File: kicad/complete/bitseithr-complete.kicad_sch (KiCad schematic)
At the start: 26 parts, among them IC1 AY-3-8912_28PIN, IC2 AY-3-8912_28PIN, J1 Power, J10 OLED Connector, J2 PWM, J3 Analog, J4 PWM, J5 Analog, J6 Communication, J7 Digital, J8 AUDIO JACK 1, J9 AUDIO JACK 2, SW1 POWER SWITCH

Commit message: schematic progress
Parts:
- removed R74: CLR, Resistor_THT:R_Axial_DIN0207_L6.3mm_D2.5mm_P10.16mm_Horizontal, symbol Device:R_Small_US
- added P1: TO KEYBOARD 1, EasyEDA_Lib:IDC-TH_20P-L33.0-W13.8-H-M-R2-C10-P2.54-S2.54-TR, symbol EasyEDA_Lib:IDC Box 2X10 2.54MM
- added R10: R_Small_US, symbol Device:R_Small_US
- added R9: 1kΩ, EasyEDA_Lib:RES-ADJ-TH_3296W, symbol EasyEDA_Lib:3296W-1-102LF
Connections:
- net 22 is gone; now on net DA0: J7.33 (Pin_33)
- net 23 is gone; now on net DA1: J7.34 (Pin_34)
- net 24 is gone; now on net DA2: J7.31 (Pin_31)
- net 25 is gone; now on net DA3: J7.32 (Pin_32)
- net 26 is gone; now on net DA4: J7.29 (Pin_29)
- net 27 is gone; now on net DA5: J7.30 (Pin_30)
- net 28 is gone; now on net DA6: J7.27 (Pin_27)
- net 29 is gone; now on net DA7: J7.28 (Pin_28)
- net A0 is gone; now on net BDIR-1: J3.1 (Pin_1)
- net A1 is gone; now on net BC1-1: J3.2 (Pin_2)
- net A2 is gone; now on net BDIR-2: J3.3 (Pin_3)
- net A3 is gone; now on net BC1-2: J3.4 (Pin_4)
- net Earth is gone; now on net GND: D73.1 (K), J8.S, J9.S, R4.2, R8.2
- net +5V: now also IC1.17 (A8), IC1.19 (BC2), IC2.19 (BC2), J10.2 (Pin_2)
- net +9V: now also P1.1
- net GND: now also IC1.6 (VSS), IC2.6 (VSS), J10.1 (Pin_1), P1.2
- net SCL/21: now also J10.4 (Pin_4)
- net SDA/20: now also J10.3 (Pin_3)
- net BDIR-1: now reaches IC1.18 (BDIR)
- net BC1-1: now reaches IC1.20 (BC1)
- net DA7: now reaches IC1.21 (DA7)
- net DA7: now also IC2.21 (DA7)
- net DA6: now reaches IC1.22 (DA6)
- net DA6: now also IC2.22 (DA6)
- net DA5: now reaches IC1.23 (DA5)
- net DA5: now also IC2.23 (DA5)
- net DA4: now reaches IC1.24 (DA4)
- net DA4: now also IC2.24 (DA4)
- net DA3: now reaches IC1.25 (DA3)
- net DA3: now also IC2.25 (DA3)
- net DA2: now reaches IC1.26 (DA2)
- net DA2: now also IC2.26 (DA2)
- net DA1: now reaches IC1.27 (DA1)
- net DA1: now also IC2.27 (DA1)
- net DA0: now reaches IC1.28 (DA0)
- net DA0: now also IC2.28 (DA0)
- net at D73.2 (A): now also R9.3
- net BDIR-2: now reaches IC2.18 (BDIR)
- net BC1-2: now reaches IC2.20 (BC1)
- new net: R10.1, R9.1, R9.2
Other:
- moved on the sheet: D73

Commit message: almost done with complete schematic
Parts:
- removed D73: POWER LED, LED_THT:LED_D3.0mm, symbol Device:LED_Small
- removed R9: 1kΩ, EasyEDA_Lib:RES-ADJ-TH_3296W, symbol EasyEDA_Lib:3296W-1-102LF
- added C25: 4.7uF-bi, Capacitor_THT:CP_Radial_D5.0mm_P2.00mm, symbol Device:CP1_Small
- added C3, C5, C8: 10 uF, Capacitor_THT:CP_Radial_D5.0mm_P2.50mm, symbol Device:CP1_Small
- added C4, C6, C7: .1 uF, caps-film:0.2_.MED, symbol Device:CP1_Small
- added J11: lil-joystick, cholm-footprints:Joystick-breakout-upside-down, symbol bit0wulf-0-rescue:psp-joystick-rect-clholm-kicad-lib
- added R13, R14, R9: 10k, symbol Device:R_Small_US
- added R22: 100k, Resistor_SMD:R_1206_3216Metric, symbol Device:R_Small_US
- added U1: ~, EasyEDA_Lib:SOIC-8_L4.9-W3.9-P1.27-LS6.0-BL, symbol EasyEDA_Lib:OPA1692IDR
- added U4: TL072, Package_SO:SOIC-8-1EP_3.9x4.9mm_P1.27mm_EP2.29x3mm, symbol Amplifier_Operational:TL072
- added VOLUME1: 100k-A, clholm-kicad-lib:16MM_T.MOUNT, symbol Device:R_POT_US
- P1: value TO KEYBOARD 1 -> SHIELD CONN 1
- R10: value R_Small_US -> 10k; now not fitted
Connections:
- net *10 is gone; now on net CLK: J2.8 (Pin_8)
- net *44 is gone; now on net ROW4: J7.11 (Pin_11)
- net *45 is gone; now on net ROW5: J7.12 (Pin_12)
- net 30 is gone; now on net RESET: J7.25 (Pin_25)
- net 31 is gone; now on net COL0: J7.26 (Pin_26)
- net 32 is gone; now on net COL1: J7.23 (Pin_23)
- net 33 is gone; now on net COL2: J7.24 (Pin_24)
- net 34 is gone; now on net COL3: J7.21 (Pin_21)
- net 35 is gone; now on net COL4: J7.22 (Pin_22)
- net 36 is gone; now on net COL5: J7.19 (Pin_19)
- net 37 is gone; now on net COL6: J7.20 (Pin_20)
- net 38 is gone; now on net COL7: J7.17 (Pin_17)
- net 39 is gone; now on net COL8: J7.18 (Pin_18)
- net 40 is gone; now on net ROW0: J7.15 (Pin_15)
- net 41 is gone; now on net ROW1: J7.16 (Pin_16)
- net 42 is gone; now on net ROW2: J7.13 (Pin_13)
- net 43 is gone; now on net ROW3: J7.14 (Pin_14)
- net VCC is gone; now on net +9V: J1.8 (Pin_8)
- net +5V: now also IC1.3 (VCC), IC2.3 (VCC), C3.1, C4.1, C6.1, C8.1, J11.1 (VCC)
- net +9V: now also C5.1, C7.1
- net BC1-1: now also R9.1
- net BC1-2: now also R13.1
- net BDIR-1: now also R10.1
- net BDIR-2: now also R14.1
- net GND: now also R10.2, C3.2, C4.2, C5.2, C6.2, C7.2, C8.2, J11.4 (GND), R13.2, R14.2, R9.2
- net CLK: now reaches IC1.15 (CLK)
- net CLK: now also IC2.15 (CLK)
- net RESET: now reaches IC1.16 (/RESET)
- net RESET: now also IC2.16 (/RESET)
- net COL1: now reaches P1.10
- net COL2: now reaches P1.11
- net COL3: now reaches P1.12
- net COL4: now reaches P1.13
- net COL5: now reaches P1.14
- net COL6: now reaches P1.15
- net COL7: now reaches P1.16
- net COL8: now reaches P1.17
- net ROW0: now reaches P1.3
- net ROW1: now reaches P1.4
- net ROW2: now reaches P1.5
- net ROW3: now reaches P1.6
- net ROW4: now reaches P1.7
- net ROW5: now reaches P1.8
- net COL0: now reaches P1.9
- net *2 renamed ECLK1
- net *3 renamed EDT1
- net +9V-IN renamed +9V IN
- net 48 renamed ESW1
- net 49 renamed ESW2
- net A4 renamed JOYX
- net JOYX: now also J11.3 (XOUT)
- net A5 renamed JOYY
- net JOYY: now also J11.2 (YOUT)
- net RX1/19 renamed EDT2
- net TX1/18 renamed ECLK2
- new net: R22.1, U4.6 (-), VOLUME1.3
- new net: C25.1, U4.7, VOLUME1.1, VOLUME1.2
- new net OUTPUT: C25.2
- new net VREF: U4.5 (+)
- no-connect marks 1 -> 5
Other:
- added sheet keyboard (keyboard.kicad_sch)
- company: (none) -> Offworld Serpent Devices
- title: (none) -> bitseithr synth
- moved on the sheet: C1, C2, D72, IC1, IC2, J8, J9, R1, R2, R3, R4, R5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

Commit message: more schematic updates
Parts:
- removed C1, C2: 100 uF, cholm-footprints:0801, symbol Device:CP1_Small
- removed C25: 4.7uF-bi, Capacitor_THT:CP_Radial_D5.0mm_P2.00mm, symbol Device:CP1_Small
- removed R22: 100k, Resistor_SMD:R_1206_3216Metric, symbol Device:R_Small_US
- removed U4: TL072, Package_SO:SOIC-8-1EP_3.9x4.9mm_P1.27mm_EP2.29x3mm, symbol Amplifier_Operational:TL072
- added C10, C12: 100uF, Capacitor_THT:CP_Radial_D6.3mm_P2.50mm, symbol Device:CP1_Small
- added C11, C13: 10uF, cholm-footprints:0801, symbol Device:CP1_Small
- added C18: .1uF, Capacitors:0805, symbol Device:C_Small
- added C21, C9: 10uF, Capacitor_THT:CP_Radial_D6.3mm_P2.50mm, symbol Device:CP1_Small
- added R15, R16: 100k, Resistor_SMD:R_1206_3216Metric, symbol Device:R_Small_US
- added R17, R18: 50k, Resistor_SMD:R_1206_3216Metric, symbol Device:R_Small_US
- added VOLUME2: 100k-A, clholm-kicad-lib:16MM_T.MOUNT, symbol Device:R_POT_US
- C3, C5, C8: value 10 uF -> 10uF
- C4, C6, C7: value .1 uF -> .1uF
- U1: value ~ -> OPA1692
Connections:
- net +5V: now also C18.1, R15.1
- net +9V: now also C9.1
- net GND: now also U1.4 (V-), C18.2, C21.2, C9.2, R16.2
- net at R1.1, R2.1, R3.1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: now also C11.1
- net OUTPUT-1: now reaches J8.T
- net OUTPUT-1: now also C10.2
- net at VOLUME1.3: now also U1.7 (OUT2), C12.1
- net at VOLUME1.1, VOLUME1.2: now also U1.6 (IN2-)
- net at U1.5 (IN2+): now also R18.1
- net at U1.1 (OUT1): now also C10.1, VOLUME2.3
- net at U1.2 (IN1-): now also VOLUME2.1, VOLUME2.2
- net at U1.3 (IN1+): now also R17.1
- net +2.5V: now reaches U1.8 (V+)
- net +2.5V: now also C21.1, R15.2, R16.1
- net at R5.1, R6.1, R7.1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: now also C13.1
- net OUTPUT-2: now reaches J9.T
- net OUTPUT-2: now also C12.2
- new net: C11.2, R17.2
- new net: C13.2, R18.2
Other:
- moved on the sheet: J11, J8, J9, U1A, U1B

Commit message: still workin. i'm crazy
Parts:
- removed C18: .1uF, Capacitors:0805, symbol Device:C_Small
- removed C9: 10uF, Capacitor_THT:CP_Radial_D6.3mm_P2.50mm, symbol Device:CP1_Small
- C21: value 10uF -> .1uF
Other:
- added sheet encoders (encoders.kicad_sch)
- moved on the sheet: C21, D72, R15, R16, SW1

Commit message: schematic continued
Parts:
- removed C21: .1uF, Capacitor_THT:CP_Radial_D6.3mm_P2.50mm, symbol Device:CP1_Small
- removed C4, C6, C7: .1uF, caps-film:0.2_.MED, symbol Device:CP1_Small
- removed R4, R8: 150R, symbol Device:R_Small_US
- added C1, C2, C4, C6: .1uF, symbol Device:C_Small
- R17, R18: value 50k -> 47k
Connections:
- net +2.5V: now also C1.1
- net +5V: now also C4.1, C6.1
- net +9V: now also C2.1
- net GND: now also C11.1, C13.1, R1.1, R2.1, R3.1, R5.1, R6.1, R7.1, C1.2, C2.2, C4.2, C6.2

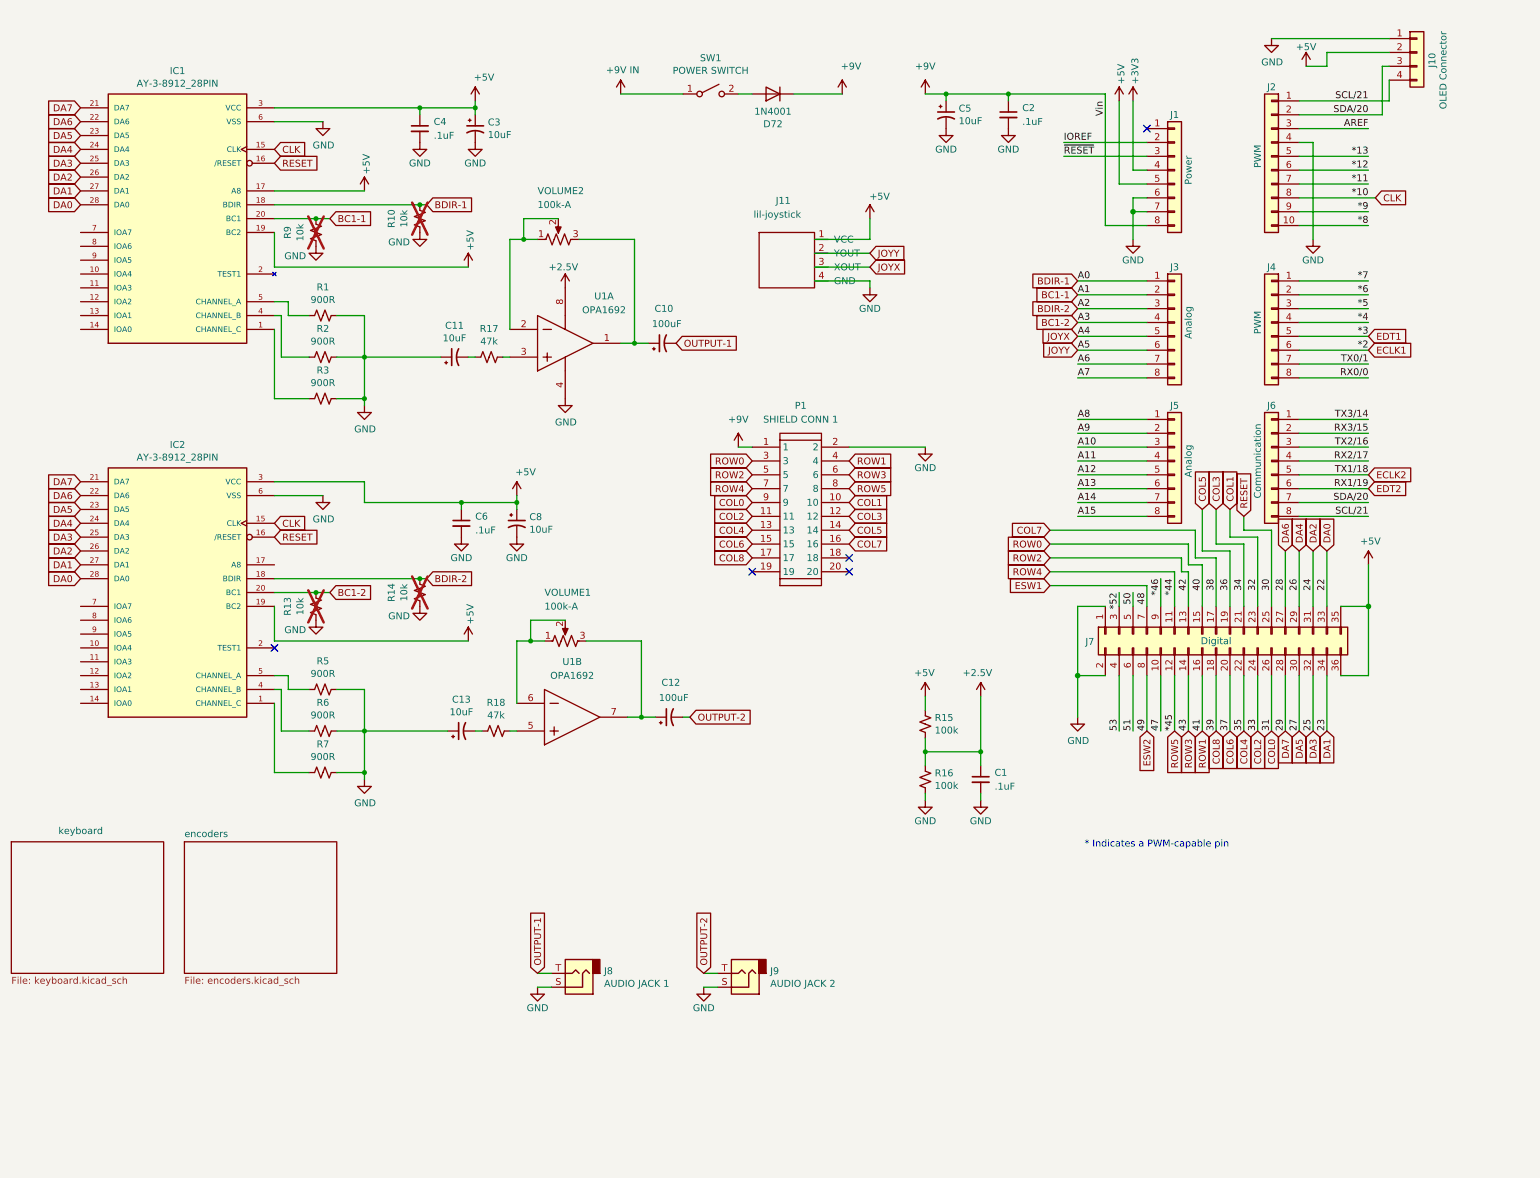
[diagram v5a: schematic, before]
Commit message: saving op-amp config before I mess with the feedback resistor
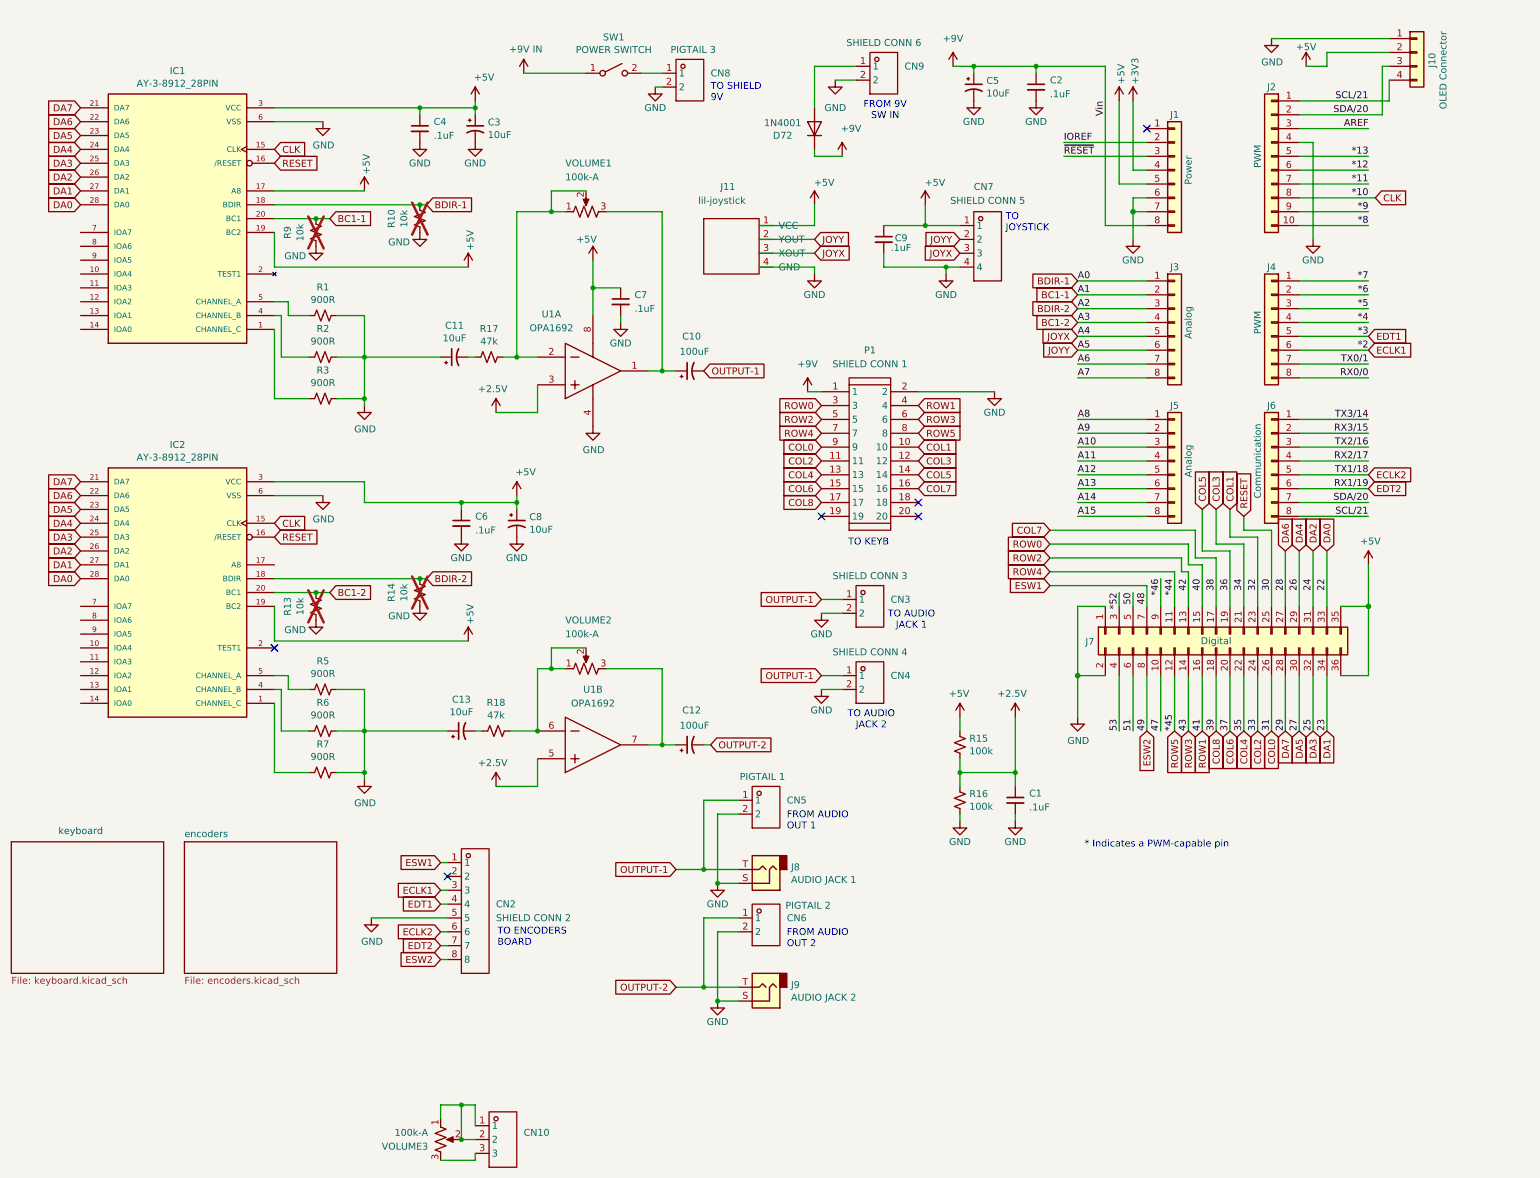
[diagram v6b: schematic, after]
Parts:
- added C7, C9: .1uF, symbol Device:C_Small
- added CN10: ~, EasyEDA_Lib:CONN-TH_3P-P2.50_HCTL_HC-XA-3AW, symbol EasyEDA_Lib:HC-XA-3AW
- added CN2: SHIELD CONN 2, EasyEDA_Lib:CONN-TH_8P-P2.50_HCTL_HC-XA-8AW, symbol EasyEDA_Lib:HC-XA-8AW
- added CN3: SHIELD CONN 3, EasyEDA_Lib:CONN-TH_2P-P2.50_HCTL_HC-XA-2AW, symbol EasyEDA_Lib:HC-XA-2AW
- added CN4: SHIELD CONN 4, EasyEDA_Lib:CONN-TH_2P-P2.50_HCTL_HC-XA-2AW, symbol EasyEDA_Lib:HC-XA-2AW
- added CN5: PIGTAIL 1, EasyEDA_Lib:CONN-TH_2P-P2.50_HCTL_HC-XA-2AW, symbol EasyEDA_Lib:HC-XA-2AW
- added CN6: PIGTAIL 2, EasyEDA_Lib:CONN-TH_2P-P2.50_HCTL_HC-XA-2AW, symbol EasyEDA_Lib:HC-XA-2AW
- added CN7: SHIELD CONN 5, EasyEDA_Lib:CONN-TH_4P-P2.50_HCTL_HC-XA-4AW, symbol EasyEDA_Lib:HC-XA-4AW
- added CN8: PIGTAIL 3, EasyEDA_Lib:CONN-TH_2P-P2.50_HCTL_HC-XA-2AW, symbol EasyEDA_Lib:HC-XA-2AW
- added CN9: SHIELD CONN 6, EasyEDA_Lib:CONN-TH_2P-P2.50_HCTL_HC-XA-2AW, symbol EasyEDA_Lib:HC-XA-2AW
- added VOLUME3: 100k-A, clholm-kicad-lib:16MM_T.MOUNT, symbol Device:R_POT_US
- renumbered VOLUME2 to VOLUME1, VOLUME1 to VOLUME2
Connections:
- net +2.5V: now also U1.3 (IN1+), U1.5 (IN2+); no longer U1.8 (V+)
- net +5V: now also U1.8 (V+), C7.1, C9.1, CN7.1
- net ECLK1: now also CN2.3
- net ECLK2: now also CN2.6
- net EDT1: now also CN2.4
- net EDT2: now also CN2.7
- net ESW1: now also CN2.1
- net ESW2: now also CN2.8
- net GND: now also C7.2, C9.2, CN2.5, CN3.2, CN4.2, CN5.2, CN6.2, CN7.4, CN8.2, CN9.2
- net JOYX: now also CN7.3
- net JOYY: now also CN7.2
- net OUTPUT-1: now also CN3.1, CN4.1, CN5.1
- net OUTPUT-2: now also CN6.1
- net at SW1.2 (B): now also CN8.1; no longer D72.2 (A)
- net at R18.1: now also U1.6 (IN2-), VOLUME2.1, VOLUME2.2; no longer U1.5 (IN2+)
- net at U1.2 (IN1-), VOLUME1.1, VOLUME1.2: now also R17.1
- new net: CN9.1, D72.2 (A)
- new net: CN10.1, CN10.2, VOLUME3.1, VOLUME3.2
- new net: CN10.3, VOLUME3.3
- no-connect marks 5 -> 6
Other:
- note added: "FROM 9V SW IN"
- note added: "FROM AUDIO OUT 1"
- note added: "FROM AUDIO OUT 2"
- note added: "TO AUDIO JACK 1"
- note added: "TO AUDIO JACK 2"
- note added: "TO ENCODERS BOARD"
- note added: "TO JOYSTICK"
- note added: "TO KEYB"
- note added: "TO SHIELD 9V"
- moved on the sheet: C1, C10, C12, C2, C5, D72, J11, J8, J9, P1, R15, R16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

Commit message: i think the schematic is done
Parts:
- removed CN10: ~, EasyEDA_Lib:CONN-TH_3P-P2.50_HCTL_HC-XA-3AW, symbol EasyEDA_Lib:HC-XA-3AW
- removed VOLUME3: 100k-A, clholm-kicad-lib:16MM_T.MOUNT, symbol Device:R_POT_US
- added CN12: SHIELD CONN 7, EasyEDA_Lib:CONN-TH_3P-P2.50_HCTL_HC-XA-3AW, symbol EasyEDA_Lib:HC-XA-3AW
- added CN14: PIGTAIL 4, EasyEDA_Lib:CONN-TH_3P-P2.50_HCTL_HC-XA-3AW, symbol EasyEDA_Lib:HC-XA-3AW
- added CN15: SHIELD CONN 8, EasyEDA_Lib:CONN-TH_3P-P2.50_HCTL_HC-XA-3AW, symbol EasyEDA_Lib:HC-XA-3AW
- added CN16: PIGTAIL 5, EasyEDA_Lib:CONN-TH_3P-P2.50_HCTL_HC-XA-3AW, symbol EasyEDA_Lib:HC-XA-3AW
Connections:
- net at R18.1, U1.6 (IN2-): now also CN15.1, CN15.2; no longer VOLUME2.1, VOLUME2.2
- net at C12.1, U1.7 (OUT2): now also CN15.3; no longer VOLUME2.3
- net at C10.1, U1.1 (OUT1): now also CN12.3; no longer VOLUME1.3
- net at R17.1, U1.2 (IN1-): now also CN12.1, CN12.2; no longer VOLUME1.1, VOLUME1.2
- new net: CN16.1, VOLUME2.1
- new net: CN16.2, VOLUME2.2
- new net: CN16.3, VOLUME2.3
- new net: CN14.1, VOLUME1.1
- new net: CN14.2, VOLUME1.2
- new net: CN14.3, VOLUME1.3
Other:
- note added: "(PIGTAILED)"
- note added: "FROM VOLUME POT 1"
- note added: "FROM VOLUME POT 2"
- note added: "TO SHIELD VOLUME 1"
- note added: "TO SHIELD VOLUME 2"
- moved on the sheet: C1, CN3, CN4, R15, R16

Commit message: erc and llm review complete
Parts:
- C11: renamed from C5; symbol Device:CP1_Small -> Device:C_Polarized_Small_US
- C2: renamed from C11; symbol Device:CP1_Small -> Device:C_Polarized_Small_US
- C4: renamed from C13; symbol Device:CP1_Small -> Device:C_Polarized_Small_US
- C5: renamed from C3; symbol Device:CP1_Small -> Device:C_Polarized_Small_US
- C6: renamed from C8; symbol Device:CP1_Small -> Device:C_Polarized_Small_US
- C8: renamed from C10; symbol Device:CP1_Small -> Device:C_Polarized_Small_US
- C9: renamed from C12; symbol Device:CP1_Small -> Device:C_Polarized_Small_US
- D1: renamed from D72; symbol Diode:1N5400 -> Diode:1N4001
- J1: renamed from J11; symbol bit0wulf-0-rescue:psp-joystick-rect-clholm-kicad-lib -> clholm-kicad-lib:psp-joystick
- J2: renamed from J8; symbol Connector:AudioJack2 -> Connector_Audio:AudioJack2
- J3: renamed from J9; symbol Connector:AudioJack2 -> Connector_Audio:AudioJack2
- VOLUME1, VOLUME2: footprint clholm-kicad-lib:16MM_T.MOUNT -> clholm-kicad-library:16MM_T.MOUNT; symbol Device:R_POT_US -> Device:R_Potentiometer_US
- renumbered C4 to C1, C9 to C10, C2 to C12, C1 to C13, C6 to C3, CN2 to CN1, CN3 to CN10, CN4 to CN11, CN7 to CN12, CN12 to CN2, CN15 to CN3, CN14 to CN4, CN8 to CN5, CN16 to CN6, CN5 to CN7, CN6 to CN8, J6 to J10, J10 to J11, J1 to J4, J3 to J5, J5 to J6, J2 to J8, J4 to J9, R9 to R1, R14 to R10, R17 to R11, R18 to R12, R15 to R13, R16 to R14, R13 to R2, R1 to R3, R2 to R4, R3 to R5, R5 to R6, R6 to R7, R7 to R8, R10 to R9
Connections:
- net +5V: now also IC2.17 (A8)
- no-connect marks 6 -> 22
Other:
- note added: "Vin"
- moved on the sheet: J1
